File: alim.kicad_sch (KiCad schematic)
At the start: 13 parts

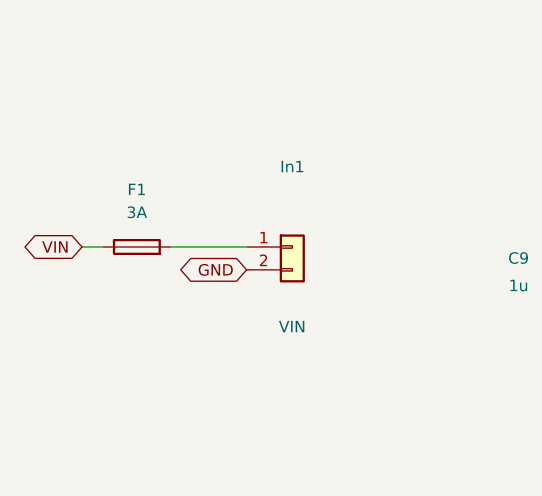
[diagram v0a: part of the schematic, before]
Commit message: Routage en cours : retouches schema (alim/flyback/isolation/limitation-courant/polarisation), doc renommage Temp_ht->I_Out_ht et NAPPE_FILAMENT_HT->DC_HT, fix .kicad_dru (commentaires #), nettoyage simulation/results
Co-Authored-By: Claude Sonnet 5 <noreply@anthropic.com>
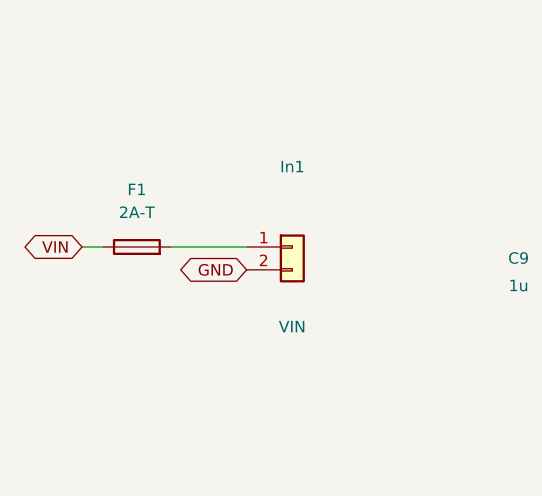
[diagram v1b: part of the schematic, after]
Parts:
- F1: value 3A -> 2A-T
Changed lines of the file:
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@@
 			)
 		)
-		(property "Value" "3A"
+		(property "Value" "2A-T"
 			(at 41.148 46.99 90)
 			(show_name no)
